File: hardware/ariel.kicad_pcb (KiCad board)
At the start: 2 copper layers, 20 parts, among them SW1 SW_Push, U1 WeMos_Battery_Shield, U2 WeMos_D1_mini, U3 74HC595, U4 Si7021_breakout

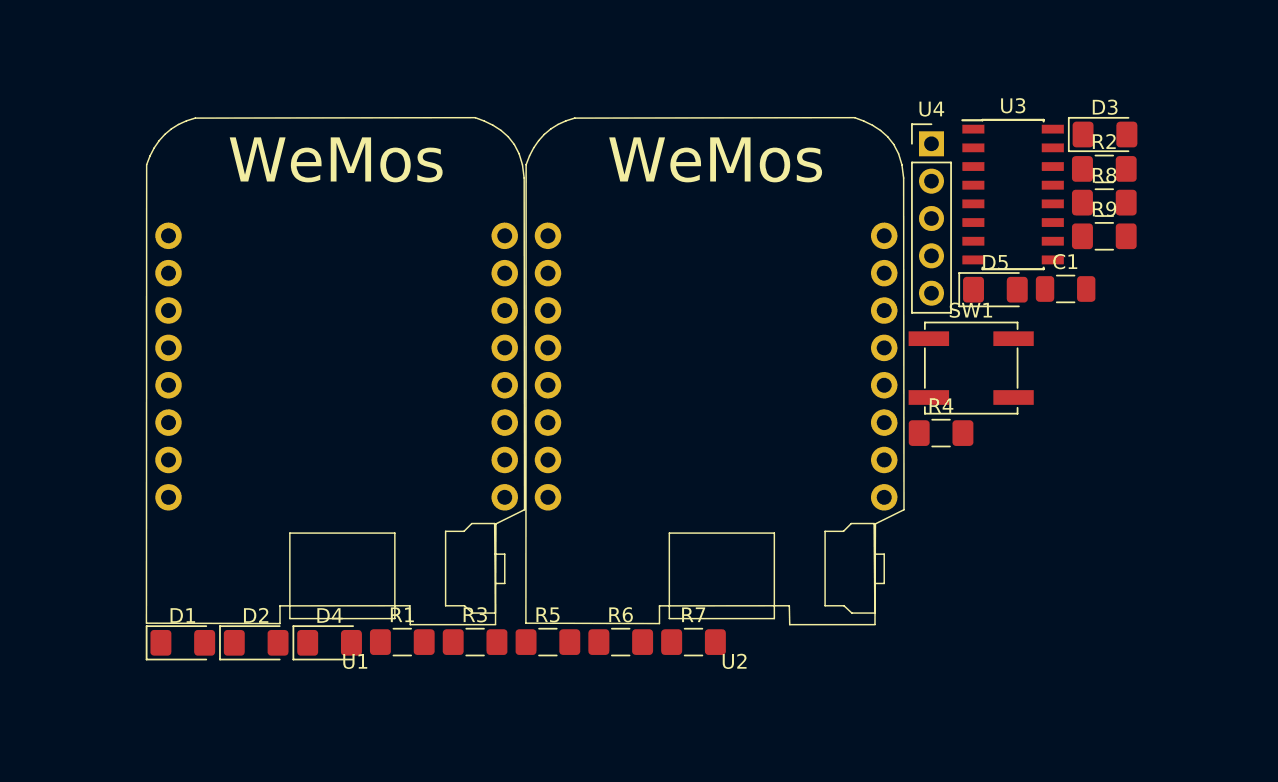
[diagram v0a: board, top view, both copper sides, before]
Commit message: Add initial footprint layout
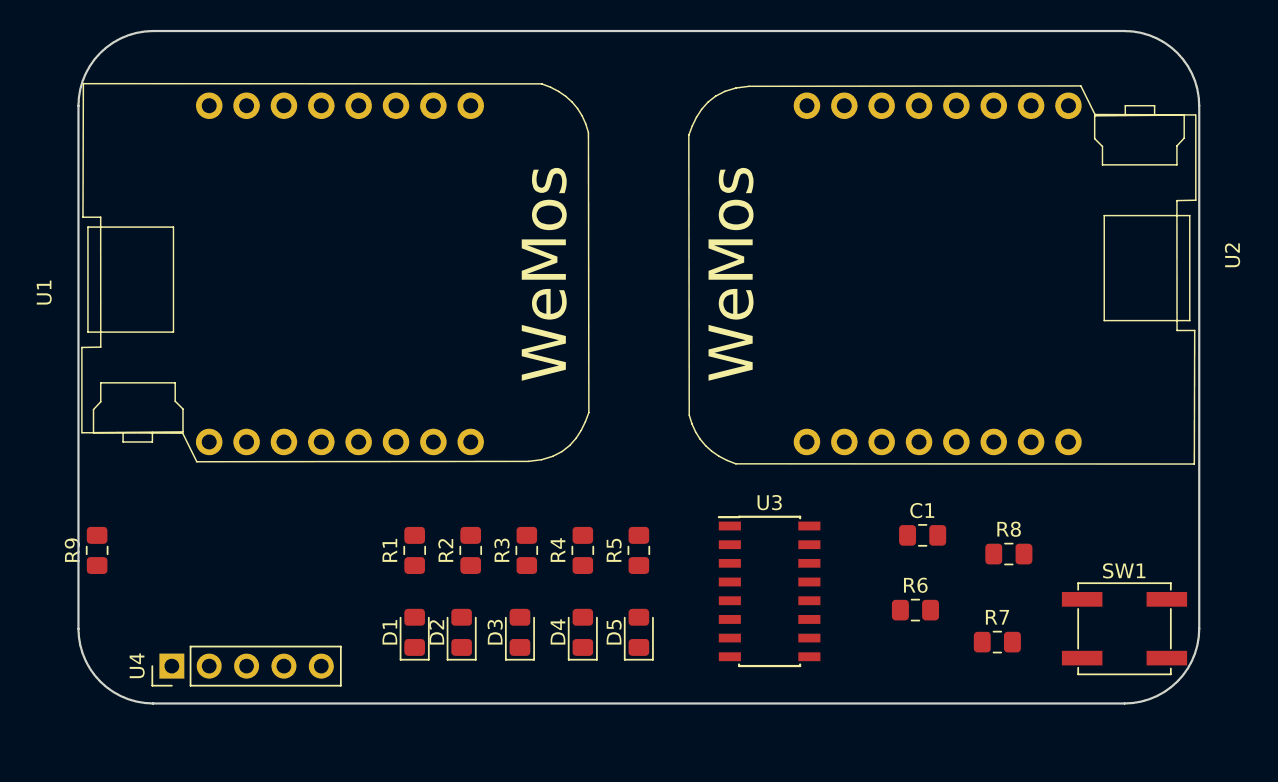
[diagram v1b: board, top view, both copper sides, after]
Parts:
- C1: footprint Capacitor_SMD:C_1206_3216Metric -> Capacitor_SMD:C_0805_2012Metric_Pad1.15x1.40mm_HandSolder
- D1, D2, D3, D4, D5: footprint LED_SMD:LED_1206_3216Metric_Pad1.42x1.75mm_HandSolder -> LED_SMD:LED_0805_2012Metric_Pad1.15x1.40mm_HandSolder
- R1, R2, R3, R4, R5, R6, R7, R8, R9: footprint Resistor_SMD:R_1206_3216Metric_Pad1.42x1.75mm_HandSolder -> Resistor_SMD:R_0805_2012Metric_Pad1.15x1.40mm_HandSolder
- moved R9 71.7 mm to (115.6, 78.5), turned to 90 degrees
- moved U4 62.7 mm to (120.7, 86.4), turned to 90 degrees
- moved D3 52.2 mm to (144.3, 84.1), turned to 90 degrees
- moved R2 50.3 mm to (141.0, 78.5), turned to 90 degrees
- moved D5 33.6 mm to (152.4, 84.1), turned to 90 degrees
- moved U3 31.7 mm to (161.3, 81.3)
- moved R4 25.6 mm to (148.6, 78.5), turned to 90 degrees
- moved R8 24.8 mm to (177.6, 78.7)
- moved R7 20.7 mm to (176.8, 84.7)
- moved SW1 20.6 mm to (185.4, 83.8)
- moved R6 20.2 mm to (171.2, 82.5)
- moved C1 19.4 mm to (171.7, 77.5)
- moved U2 18.0 mm to (174.0, 59.7), turned to 90 degrees
- moved D4 17.2 mm to (148.6, 84.1), turned to 90 degrees
- moved D1 15.8 mm to (137.2, 84.1), turned to 90 degrees
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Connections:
- U1 pad 11: Net-(U1-Pad11) -> (no net)
- U1 pad 12: Net-(U1-Pad12) -> (no net)
- U1 pad 13: Net-(U1-Pad13) -> (no net)
- U1 pad 14: Net-(U1-Pad14) -> (no net)
- U1 pad 15: Net-(U1-Pad15) -> (no net)
- U1 pad 16: Net-(U1-Pad16) -> (no net)
- U1 pad 3: Net-(U1-Pad3) -> (no net)
- U1 pad 4: Net-(U1-Pad4) -> (no net)
- U1 pad 5: Net-(U1-Pad5) -> (no net)
- U1 pad 6: Net-(U1-Pad6) -> (no net)
- U1 pad 7: Net-(U1-Pad7) -> (no net)
- U1 pad 8: Net-(U1-Pad8) -> (no net)
- U1 pad 9: Net-(U1-Pad9) -> (no net)
- U2 pad 4: Net-(U2-Pad4) -> (no net)
- U2 pad 7: Net-(U2-Pad7) -> (no net)
- U2 pad 8: Net-(U2-Pad8) -> (no net)
- U3 pad 5: Net-(U3-Pad5) -> (no net)
- U3 pad 6: Net-(U3-Pad6) -> (no net)
- U3 pad 7: Net-(U3-Pad7) -> (no net)
- U3 pad 9: Net-(U3-Pad9) -> (no net)
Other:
- board outline added: 76.2 x 45.7 mm

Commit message: Tweak WeMos battery shield footprint
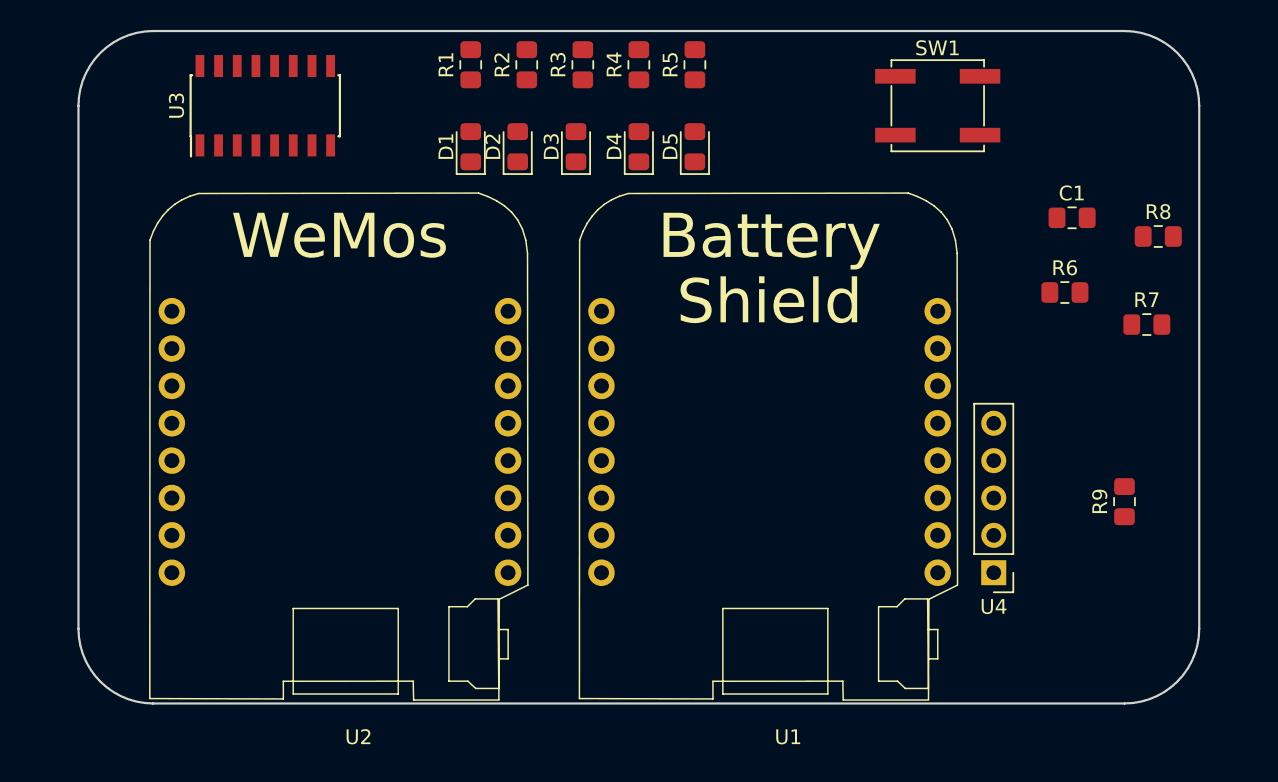
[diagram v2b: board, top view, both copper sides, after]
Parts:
- U1: footprint WeMos:D1_mini_board -> WeMos:Battery_shield
- moved R9 69.9 mm to (185.4, 75.2)
- moved U4 56.2 mm to (176.5, 80.0), turned to 180 degrees
- moved U3 47.6 mm to (127.0, 48.3), turned to 90 degrees
- moved U2 43.8 mm to (132.1, 72.4), turned to 0 degrees
- moved SW1 37.8 mm to (172.7, 48.3)
- moved R1 33.2 mm to (141.0, 45.5)
- moved R2 33.2 mm to (144.8, 45.5)
- moved R3 33.2 mm to (148.6, 45.5)
- moved R4 33.2 mm to (152.4, 45.5)
- moved R5 33.2 mm to (156.2, 45.5)
- moved D1 33.2 mm to (141.0, 51.0)
- moved D2 33.2 mm to (144.2, 51.0)
- moved D3 33.2 mm to (148.1, 51.0)
- moved D4 33.2 mm to (152.4, 51.0)
- moved D5 33.2 mm to (156.2, 51.0)
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
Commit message: Edit footprint for battery shield and wemos board
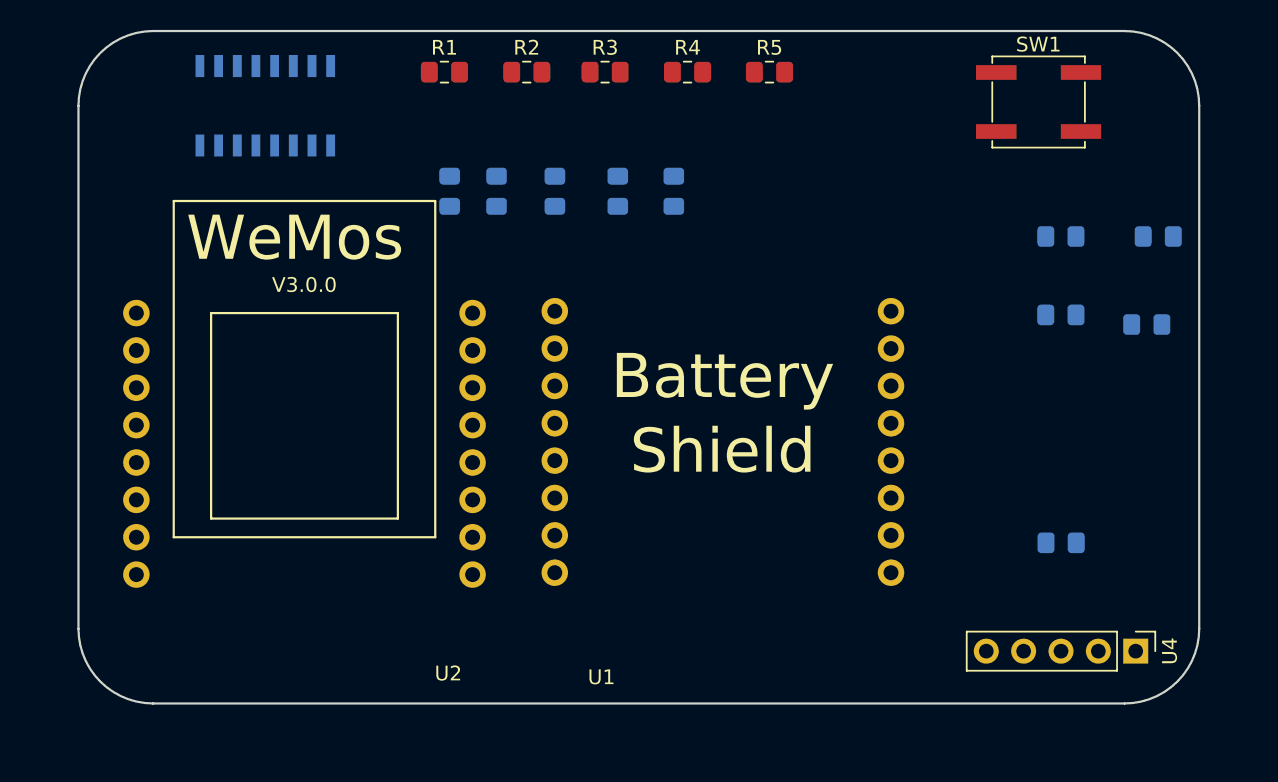
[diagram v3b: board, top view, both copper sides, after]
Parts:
- C1, D1, D2, D3, D4, D5, R6, R7, R8, R9, U3: moved to B.Cu
- moved U4 11.0 mm to (186.2, 85.3), turned to 270 degrees
- moved SW1 6.86 mm to (179.6, 48.0)
- moved R9 5.14 mm to (181.1, 78.0), turned to 180 degrees
- moved R5 5.10 mm to (161.3, 46.0), turned to 0 degrees
- moved U1 3.41 mm to (158.2, 73.9)
- moved D1 3.35 mm to (139.5, 54.1), turned to 270 degrees
- moved D2 3.35 mm to (142.7, 54.1), turned to 270 degrees
- moved D3 3.35 mm to (146.7, 54.1), turned to 270 degrees
- moved D4 3.35 mm to (151.0, 54.1), turned to 270 degrees
- moved D5 3.35 mm to (154.8, 54.1), turned to 270 degrees
- moved R4 3.35 mm to (155.7, 46.0), turned to 0 degrees
- moved U2 2.51 mm to (130.3, 70.6)
- moved R1 1.86 mm to (139.2, 46.0), turned to 0 degrees
- moved R3 1.60 mm to (150.1, 46.0), turned to 0 degrees
- moved R6 1.55 mm to (181.1, 62.5)
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
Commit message: Layout tracks and fix footprint
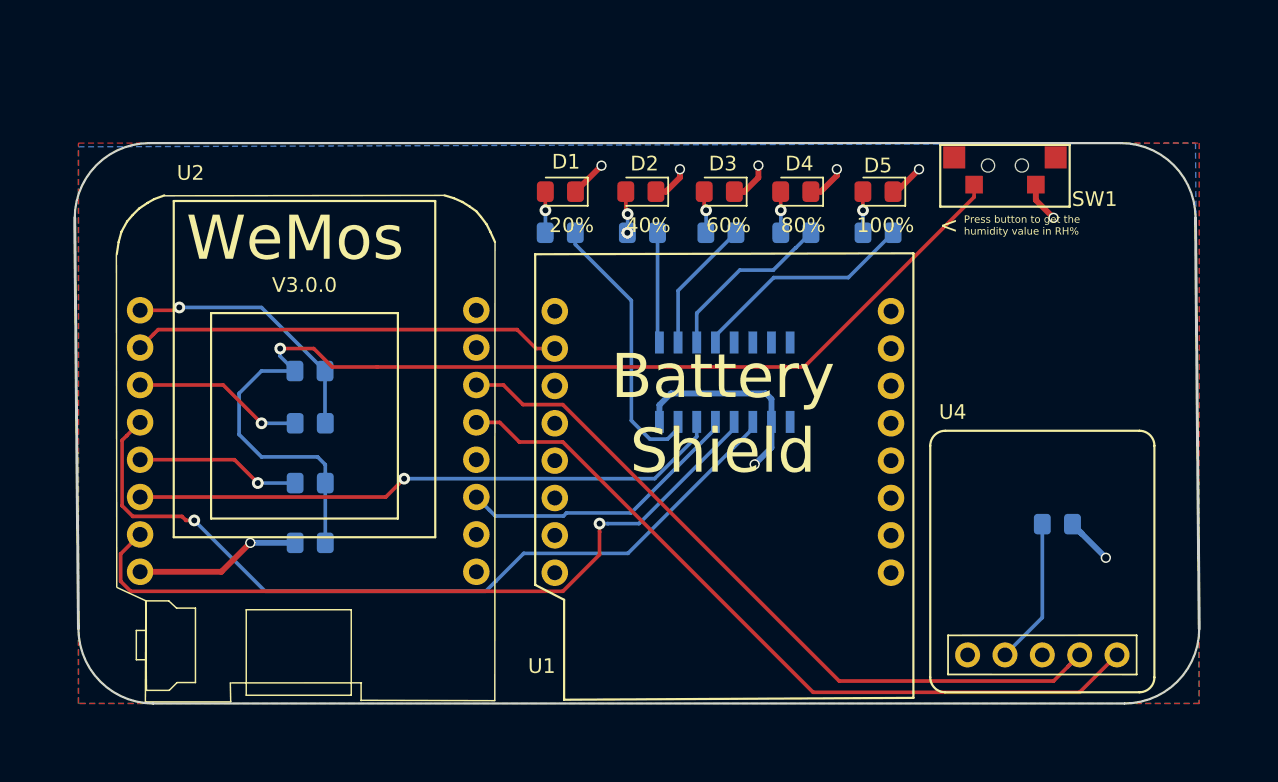
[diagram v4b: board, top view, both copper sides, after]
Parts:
- D1, D2, D3, D4, D5: moved to F.Cu
- R1, R2, R3, R4, R5: moved to B.Cu
- SW1: footprint Button_Switch_SMD:SW_SPST_EVPBF -> Switch_Tactile_pushbutton:Tactile_pushbutton
- U4: footprint Connector_PinHeader_2.54mm:PinHeader_1x05_P2.54mm_Vertical -> Si7021:Si7021_breakout_board
- moved R8 61.3 mm to (130.1, 78.0), turned to 180 degrees
- moved R7 57.9 mm to (130.1, 73.9), turned to 180 degrees
- moved C1 51.9 mm to (130.0, 66.3), turned to 180 degrees
- moved R6 51.6 mm to (130.1, 69.8), turned to 180 degrees
- moved U3 36.5 mm to (158.2, 67.1)
- moved D5 13.9 mm to (168.7, 54.1), turned to 180 degrees
- moved R3 13.5 mm to (158.0, 56.9), turned to 180 degrees
- moved R1 13.5 mm to (147.1, 56.9), turned to 180 degrees
- moved R2 13.5 mm to (152.6, 56.9), turned to 180 degrees
- moved R5 13.2 mm to (168.7, 56.9), turned to 180 degrees
- moved R4 13.2 mm to (163.1, 56.9), turned to 180 degrees
- moved D4 12.1 mm to (163.1, 54.1), turned to 180 degrees
- moved D3 11.2 mm to (157.9, 54.1), turned to 180 degrees
- moved D2 9.81 mm to (152.5, 54.1), turned to 180 degrees
- moved U4 8.80 mm to (179.8, 79.2), turned to 0 degrees
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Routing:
- net Net-(C1-Pad2): track 0.00 -> 74.5 mm, vias 0 -> 1
- net /D5: track 0.00 -> 56.5 mm, vias 0 -> 1
- net /I2C_SDA: track 0.00 -> 52.2 mm
- net /D8: track 0.00 -> 52.0 mm, vias 0 -> 1
- net /I2C_SCL: track 0.00 -> 51.3 mm
- net /D7: track 0.00 -> 40.5 mm, vias 0 -> 1
- net /A0: track 0.00 -> 29.2 mm
- net /EN: track 0.00 -> 19.7 mm
- net /QA: track 0.00 -> 19.2 mm
- net VCC: track 0.00 -> 18.3 mm, vias 0 -> 2
- net /RST: track 0.00 -> 18.0 mm, vias 0 -> 1
- net GND: track 0.00 -> 15.8 mm, vias 0 -> 6
- net /QE: track 0.00 -> 15.4 mm
- net /QD: track 0.00 -> 12.0 mm
- net /D0: track 0.00 -> 11.6 mm, vias 0 -> 1
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- added copper zone on B.Cu, net GND
- added copper zone on F.Cu, net VCC
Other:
- board size 76.2 x 45.7 mm -> 76.5 x 38.1 mm
- net class Power added: clearance 0.3, trace_width 0.4, via_dia 0.7, via_drill 0.5
- board text added: "100%"
- board text added: "20%"
- board text added: "40%"
- board text added: "60%"
- board text added: "80%"
- board text added: "<"
- board text added: "Press button to get the humidity value in RH%"
- board text added: "Si7021 board"

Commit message: Pass ERC
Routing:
- net /I2C_SDA: track 52.2 -> 67.0 mm
- net /I2C_SCL: track 51.3 -> 66.1 mm
- net /D5: track 56.5 -> 57.6 mm
- net /QE: track 15.4 -> 16.2 mm

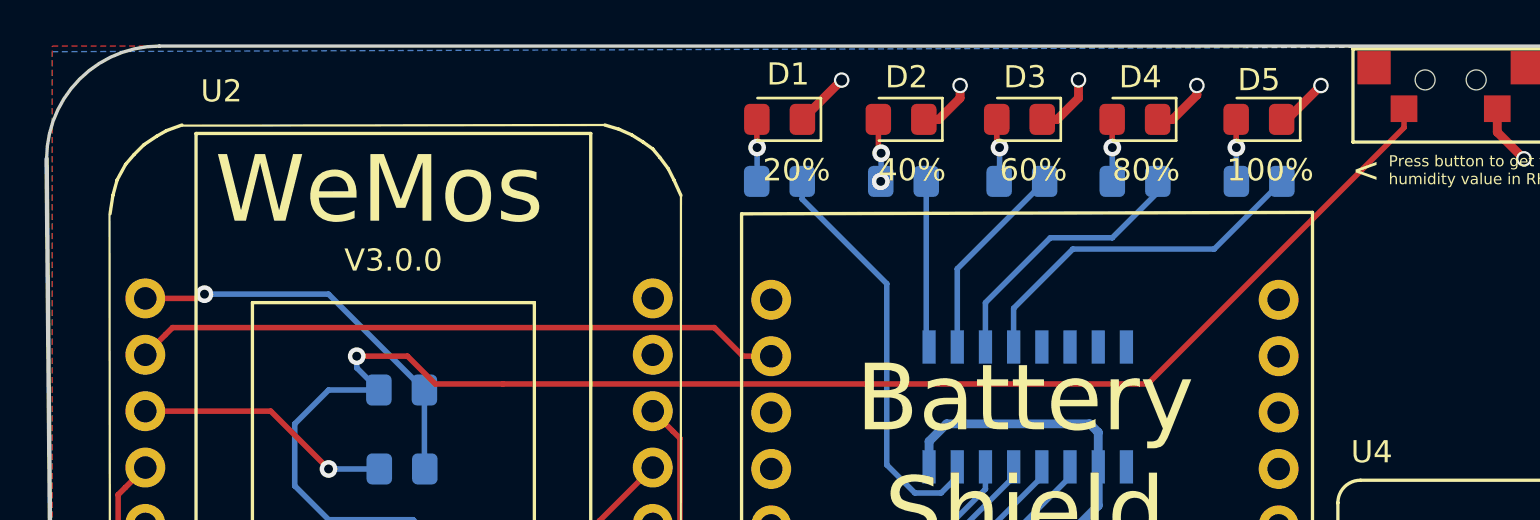
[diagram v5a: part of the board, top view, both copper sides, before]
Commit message: Add OSHW logo, expand copper fill zones
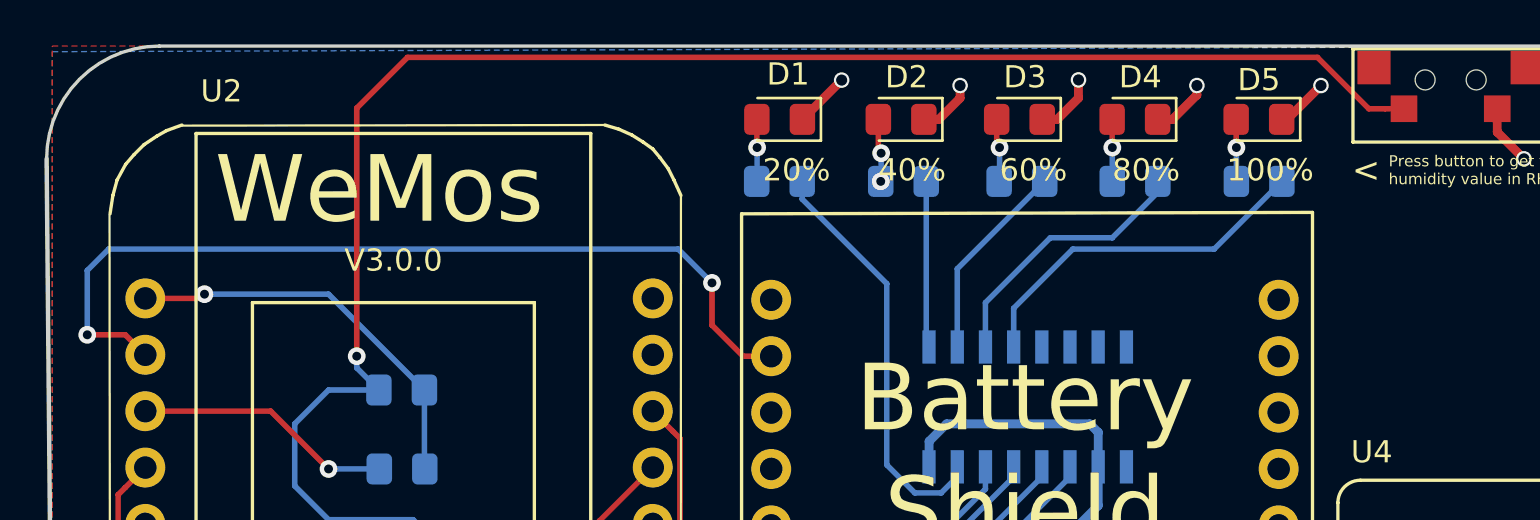
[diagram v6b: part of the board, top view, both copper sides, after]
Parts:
- added REF**: OSHW-Logo2_7.3x6mm_SilkScreen, Symbol:OSHW-Logo2_7.3x6mm_SilkScreen, B.Cu at (180.3, 63.5)
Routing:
- net /A0: track 29.2 -> 40.2 mm, vias 0 -> 2
- net Net-(C1-Pad2): track 74.5 -> 81.4 mm
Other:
- board text added: "Cactus@Hutscape V1.0 2019"
- board text added: "Get started at: https://hutscape.com/cactus"
